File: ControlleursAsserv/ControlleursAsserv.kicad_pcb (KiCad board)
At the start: 4 copper layers, 85 x 56 mm, 100 parts, among them J1 I2C1_5, J10 Codeur, J11 Motor FeedBack, J12 Motor CMD, J13 Codeur, J14 Motor FeedBack, J15 Motor CMD, J16 Codeur, J17 Motor FeedBack, J18 Motor CMD, J2 I2C2_5, J3 CAN1, J4 CAN2, J5 In App Prog, J6 DEBUG, J7 Codeur, J8 Motor CMD, J9 Motor FeedBack, Q1 BSS138, Q10 BSS138, Q11 BSS138, Q12 BSS138, Q13 BSS138, Q14 BSS138, Q2 BSS138, Q3 BSS138, Q4 BSS138, Q5 BSS138, Q6 BSS138, Q7 BSS138, Q8 BSS138, Q9 BSS138, SW1 RESET, SW2 BOOT0, U1 STM32G474RETx, U2 AMS1117-3.3, U3 MCP2558FD-xSN, Y1 16MHz

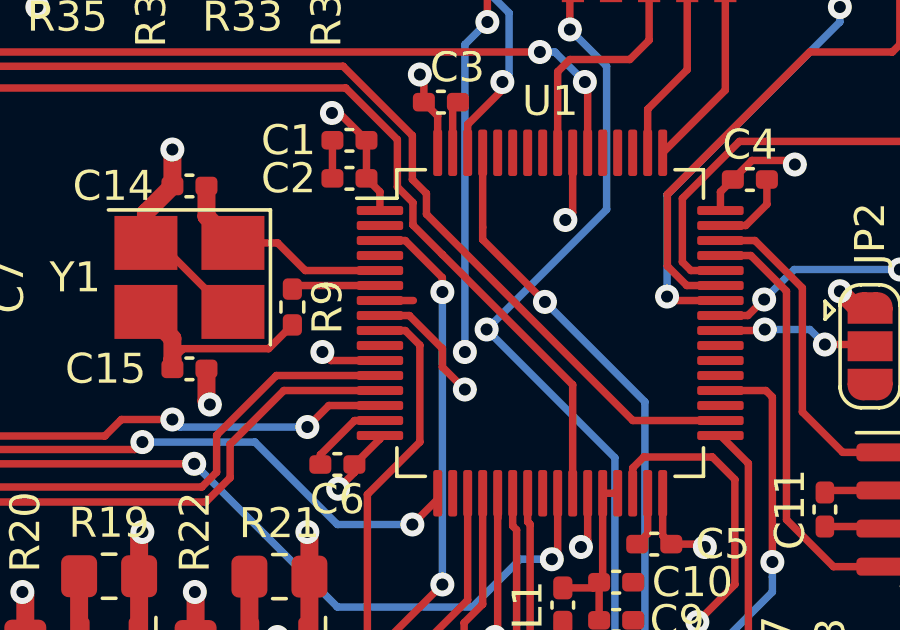
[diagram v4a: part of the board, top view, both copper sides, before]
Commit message: Add size value in layer comments
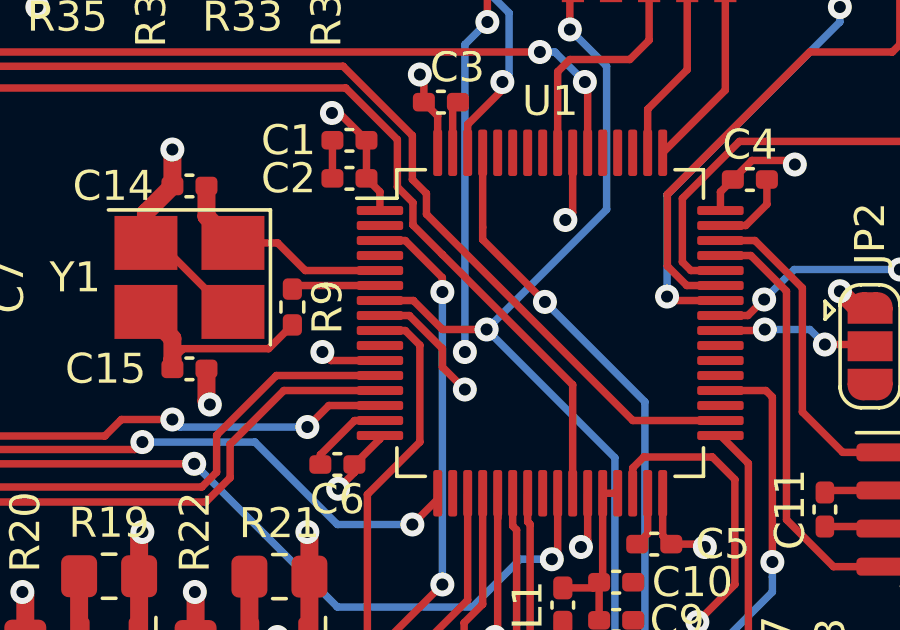
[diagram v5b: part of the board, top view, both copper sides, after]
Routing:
- net RESET: track 53.1 -> 56.0 mm
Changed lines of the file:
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@@
   )
   (dimension (type aligned) (layer "Cmts.User")
-    (pts (xy 145.75 38.75) (xy 145.75 94.75))
-    (height -4.25)
-    (gr_text "56.0000 mm" (at 148.85 66.75 90) (layer "Cmts.User")
+    (pts (xy 64.25 42.25) (xy 64.25 91.25))
+    (height 6.499999)
+    (gr_text "49.0000 mm" (at 56.600001 66.75 90) (layer "Cmts.User")
       (effects (font (size 1 1) (thickness 0.15)))
     )
@@
   )
   (dimension (type aligned) (layer "Cmts.User")
+    (pts (xy 145.75 38.75) (xy 145.75 94.75))
+    (height -11.75)
+    (gr_text "56.0000 mm" (at 156.35 66.75 90) (layer "Cmts.User")
+      (effects (font (size 1 1) (thickness 0.15)))
+    )
+    (format (prefix "") (suffix "") (units 3) (units_format 1) (precision 4))
+    (style (thickness 0.15) (arrow_length 1.27) (text_position_mode 0) (extension_height 0.58642) (extension_offset 0.5) keep_text_aligned)
+  )
+  (dimension (type aligned) (layer "Cmts.User")
+    (pts (xy 64.25 42.25) (xy 122.25 42.25))
+    (height -8)
+    (gr_text "58.0000 mm" (at 93.25 33.1) (layer "Cmts.User")
+      (effects (font (size 1 1) (thickness 0.15)))
+    )
+    (format (prefix "") (suffix "") (units 3) (units_format 1) (precision 4))
+    (style (thickness 0.15) (arrow_length 1.27) (text_position_mode 0) (extension_height 0.58642) (extension_offset 0.5) keep_text_aligned)
+  )
+  (dimension (type aligned) (layer "Cmts.User")
     (pts (xy 60.75 38.75) (xy 145.75 38.75))
-    (height -4.75)
-    (gr_text "85.0000 mm" (at 103.25 32.85) (layer "Cmts.User")
+    (height -10)
+    (gr_text "85.0000 mm" (at 103.25 27.6) (layer "Cmts.User")
       (effects (font (size 1 1) (thickness 0.15)))
     )
@@
   (segment (start 111.169 67.534) (end 112.284 67.534) (width 0.25) (layer "F.Cu") (net 5))
   (segment (start 136.4855 88.42) (end 136.906 88.8405) (width 0.25) (layer "F.Cu") (net 5))
+  (segment (start 113.249019 68.499019) (end 114.725 68.499019) (width 0.25) (layer "F.Cu") (net 5))
   (segment (start 126.0299 86.25) (end 123.75 86.25) (width 0.25) (layer "F.Cu") (net 5))
   (segment (start 117.5 58.5) (end 117.5 56.49) (width 0.25) (layer "F.Cu") (net 5))
+  (segment (start 112.284 67.534) (end 113.249019 68.499019) (width 0.25) (layer "F.Cu") (net 5))
   (segment (start 117.5 56.49) (end 117.602 56.388) (width 0.25) (layer "F.Cu") (net 5))
   (segment (start 128.54 86.25) (end 126.0299 86.25) (width 0.25) (layer "F.Cu") (net 5))

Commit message: Finish Controller Asserv
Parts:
- added C16: 100n, Capacitor_SMD:C_0402_1005Metric_Pad0.74x0.62mm_HandSolder, F.Cu at (131.3, 77.8)
- moved C15 1.32 mm to (103.5, 69.8), turned to 180 degrees
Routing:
- net FAULT_1: track 3.25 -> 60.7 mm, vias 0 -> 3
- net FAULT_2: track 3.25 -> 58.0 mm, vias 0 -> 2
- net SLEEP_3: track 0.00 -> 48.3 mm, vias 0 -> 1
- net PWM_3: track 0.00 -> 39.1 mm, vias 0 -> 1
- net DIR_3: track 0.00 -> 35.8 mm, vias 0 -> 1
- net SLEEP_4: track 0.00 -> 32.8 mm, vias 0 -> 1
- net DIR_1: track 12.5 -> 40.9 mm, vias 0 -> 2
- net CHB_4: track 2.13 -> 28.9 mm, vias 0 -> 2
- net IDX_4: track 2.13 -> 25.5 mm, vias 0 -> 2
- net CHA_4: track 2.13 -> 23.3 mm, vias 0 -> 2
- net GND: track 22.8 -> 42.8 mm, vias 3 -> 8
- net +5V: track 32.9 -> 48.1 mm, vias 13 -> 19
- net PWM_4: track 28.8 -> 25.5 mm, vias 3 -> 1
- net +3.3V: track 120.0 -> 123.3 mm, vias 48 -> 49
- net DIR_4: track 17.0 -> 15.7 mm, vias 2 -> 0
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
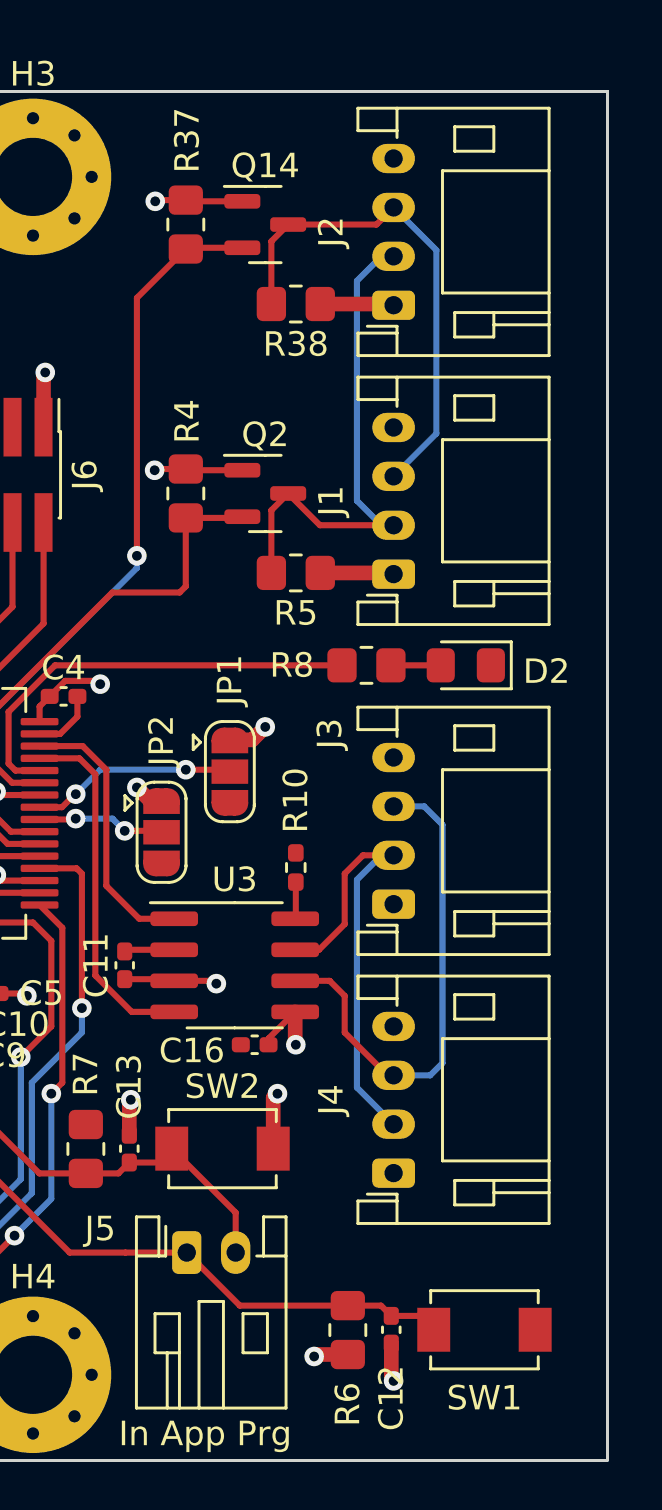
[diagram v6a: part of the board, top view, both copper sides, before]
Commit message: Fix CAN connections to improve routing on ControllerAsserv
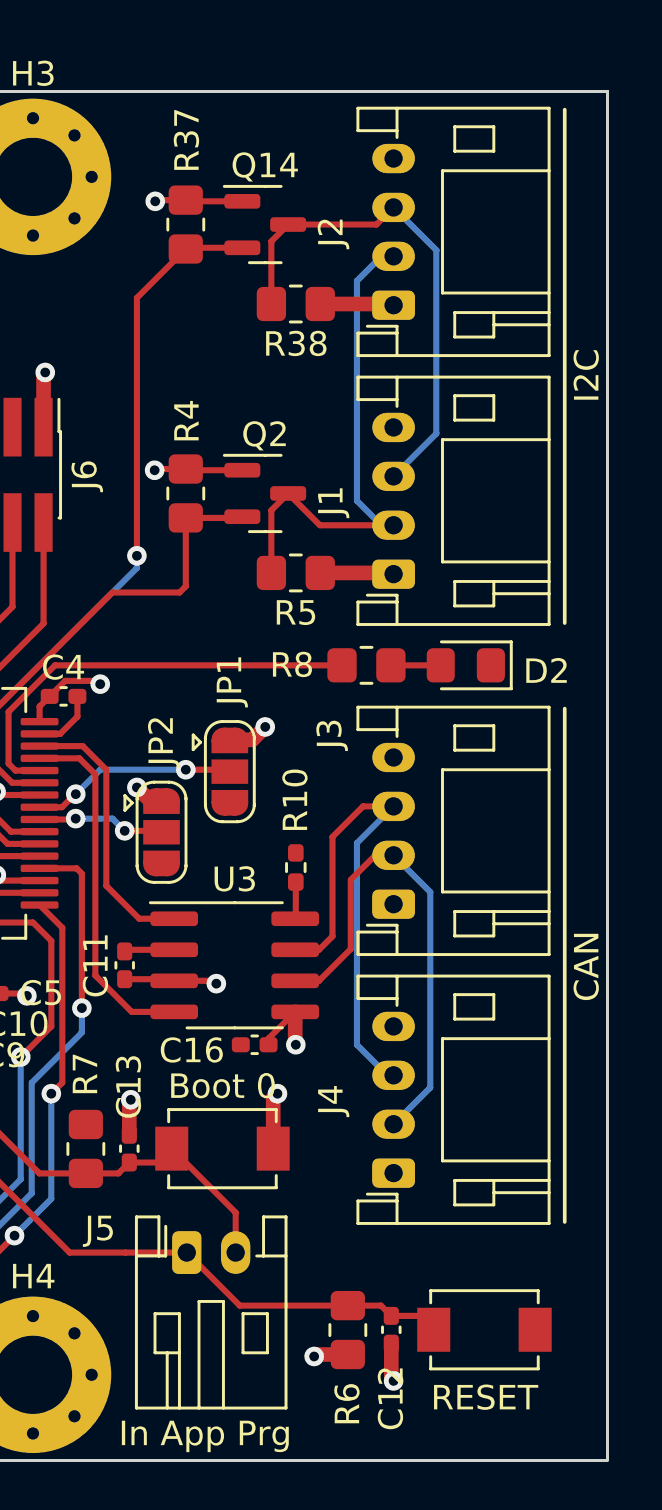
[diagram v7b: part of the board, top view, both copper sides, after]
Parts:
- Boot 0: renamed from SW2
- renumbered SW1 to RESET
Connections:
- U3 pad 6: Net-(J3-Pin_3) -> Net-(J3-Pin_2)
- U3 pad 7: Net-(J3-Pin_2) -> Net-(J3-Pin_3)
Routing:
- net Net-(J3-Pin_2): track 19.4 -> 20.6 mm
- net Net-(J3-Pin_3): track 20.8 -> 21.5 mm
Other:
- board text added: "CAN"
- board text added: "I2C"
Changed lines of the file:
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@@
     (property "ki_keywords" "switch normally-open pushbutton push-button")
     (attr smd)
-    (fp_text reference "SW1" (at 0 -2.794) (layer "F.SilkS")
+    (fp_text reference "RESET" (at 0 -2.794) (layer "F.SilkS")
         (effects (font (size 1 1) (thickness 0.15)))
     )
@@
       (net 1 "+3.3V") (pinfunction "VIO") (pintype "power_in"))
     (pad "6" smd roundrect (at 2.475 0.635) (size 1.95 0.6) (layers "F.Cu" "F.Paste" "F.Mask") (roundrect_rratio 0.25)
-      (net 14 "Net-(J3-Pin_3)") (pinfunction "CANL") (pintype "bidirectional"))
+      (net 13 "Net-(J3-Pin_2)") (pinfunction "CANL") (pintype "bidirectional"))
     (pad "7" smd roundrect (at 2.475 -0.635) (size 1.95 0.6) (layers "F.Cu" "F.Paste" "F.Mask") (roundrect_rratio 0.25)
-      (net 13 "Net-(J3-Pin_2)") (pinfunction "CANH") (pintype "bidirectional"))
+      (net 14 "Net-(J3-Pin_3)") (pinfunction "CANH") (pintype "bidirectional"))
     (pad "8" smd roundrect (at 2.475 -1.905) (size 1.95 0.6) (layers "F.Cu" "F.Paste" "F.Mask") (roundrect_rratio 0.25)
       (net 70 "Net-(U3-S)") (pinfunction "S") (pintype "input"))
@@
     (property "ki_keywords" "switch normally-open pushbutton push-button")
     (attr smd)
-    (fp_text reference "SW2" (at 0 -2.54) (layer "F.SilkS")
+    (fp_text reference "Boot 0" (at 0 -2.54) (layer "F.SilkS")
         (effects (font (size 1 1) (thickness 0.15)))
     )
@@
     )
   )
+  (gr_line (start 144 39.5) (end 144 60.5)
+    (stroke (width 0.15) (type default)) (layer "F.SilkS"))
+  (gr_line (start 144 64) (end 144 85)
+    (stroke (width 0.15) (type default)) (layer "F.SilkS"))
   (gr_rect (start 60.75 38.75) (end 145.75 94.75)
     (stroke (width 0.1) (type default)) (fill none) (layer "Edge.Cuts"))
@@
     (effects (font (size 1 1) (thickness 0.15)) (justify left bottom))
   )
+  (gr_text "CAN" (at 145.5 76 90) (layer "F.SilkS")
+    (effects (font (size 1 1) (thickness 0.15)) (justify left bottom))
+  )
+  (gr_text "I2C" (at 145.5 51.5 90) (layer "F.SilkS")
+    (effects (font (size 1 1) (thickness 0.15)) (justify left bottom))
+  )
   (dimension (type aligned) (layer "Cmts.User")
     (pts (xy 64.25 42.25) (xy 64.25 91.25))
@@
   (segment (start 137 43.5) (end 138.75 45.25) (width 0.25) (layer "B.Cu") (net 12))
   (segment (start 138.75 45.25) (end 138.75 52.75) (width 0.25) (layer "B.Cu") (net 12))
-  (segment (start 135 70.75) (end 135.75 70) (width 0.25) (layer "F.Cu") (net 13))
-  (segment (start 135.75 70) (end 137 70) (width 0.25) (layer "F.Cu") (net 13))
-  (segment (start 135 72.814999) (end 135 70.75) (width 0.25) (layer "F.Cu") (net 13))
-  (segment (start 132.975 73.865) (end 133.949999 73.865) (width 0.25) (layer "F.Cu") (net 13))
-  (segment (start 133.949999 73.865) (end 135 72.814999) (width 0.25) (layer "F.Cu") (net 13))
+  (segment (start 132.975 75.135) (end 133.949999 75.135) (width 0.25) (layer "F.Cu") (net 13))
+  (segment (start 136.25 70) (end 137 70) (width 0.25) (layer "F.Cu") (net 13))
+  (segment (start 135.25 73.834999) (end 135.25 71) (width 0.25) (layer "F.Cu") (net 13))
+  (segment (start 133.949999 75.135) (end 135.25 73.834999) (width 0.25) (layer "F.Cu") (net 13))
+  (segment (start 135.25 71) (end 136.25 70) (width 0.25) (layer "F.Cu") (net 13))
+  (segment (start 138.5 71.5) (end 138.5 79.5) (width 0.25) (layer "B.Cu") (net 13))
   (segment (start 137 70) (end 136.5 70) (width 0.25) (layer "B.Cu") (net 13))
-  (segment (start 135.5 71) (end 135.5 79.5) (width 0.25) (layer "B.Cu") (net 13))
-  (segment (start 136.5 70) (end 135.5 71) (width 0.25) (layer "B.Cu") (net 13))
-  (segment (start 135.5 79.5) (end 137 81) (width 0.25) (layer "B.Cu") (net 13))
-  (segment (start 134.385 75.135) (end 135 75.75) (width 0.25) (layer "F.Cu") (net 14))
-  (segment (start 135 75.75) (end 135 77.25) (width 0.25) (layer "F.Cu") (net 14))
-  (segment (start 135 77.25) (end 136.75 79) (width 0.25) (layer "F.Cu") (net 14))
-  (segment (start 132.975 75.135) (end 134.385 75.135) (width 0.25) (layer "F.Cu") (net 14))
+  (segment (start 137 70) (end 138.5 71.5) (width 0.25) (layer "B.Cu") (net 13))
+  (segment (start 138.5 79.5) (end 137 81) (width 0.25) (layer "B.Cu") (net 13))
+  (segment (start 135.75 68) (end 137 68) (width 0.25) (layer "F.Cu") (net 14))
+  (segment (start 134.5 73.314999) (end 134.5 69.25) (width 0.25) (layer "F.Cu") (net 14))
+  (segment (start 133.949999 73.865) (end 134.5 73.314999) (width 0.25) (layer "F.Cu") (net 14))
+  (segment (start 132.975 73.865) (end 133.949999 73.865) (width 0.25) (layer "F.Cu") (net 14))
+  (segment (start 134.5 69.25) (end 135.75 68) (width 0.25) (layer "F.Cu") (net 14))
   (segment (start 136.75 79) (end 137 79) (width 0.25) (layer "F.Cu") (net 14))
-  (segment (start 139 68.75) (end 139 78.5) (width 0.25) (layer "B.Cu") (net 14))
-  (segment (start 139 78.5) (end 138.5 79) (width 0.25) (layer "B.Cu") (net 14))
-  (segment (start 137 68) (end 138.25 68) (width 0.25) (layer "B.Cu") (net 14))
-  (segment (start 138.25 68) (end 139 68.75) (width 0.25) (layer "B.Cu") (net 14))
-  (segment (start 138.5 79) (end 137 79) (width 0.25) (layer "B.Cu") (net 14))
+  (segment (start 137 68) (end 135.5 69.5) (width 0.25) (layer "B.Cu") (net 14))
+  (segment (start 135.5 69.5) (end 135.5 77.75) (width 0.25) (layer "B.Cu") (net 14))
+  (segment (start 135.5 77.75) (end 136.75 79) (width 0.25) (layer "B.Cu") (net 14))
+  (segment (start 136.75 79) (end 137 79) (width 0.25) (layer "B.Cu") (net 14))
   (segment (start 122.682 56.388) (end 122.682 60.521) (width 0.25) (layer "F.Cu") (net 15))
   (segment (start 122.682 60.521) (end 120.594 62.609) (width 0.25) (layer "F.Cu") (net 15))

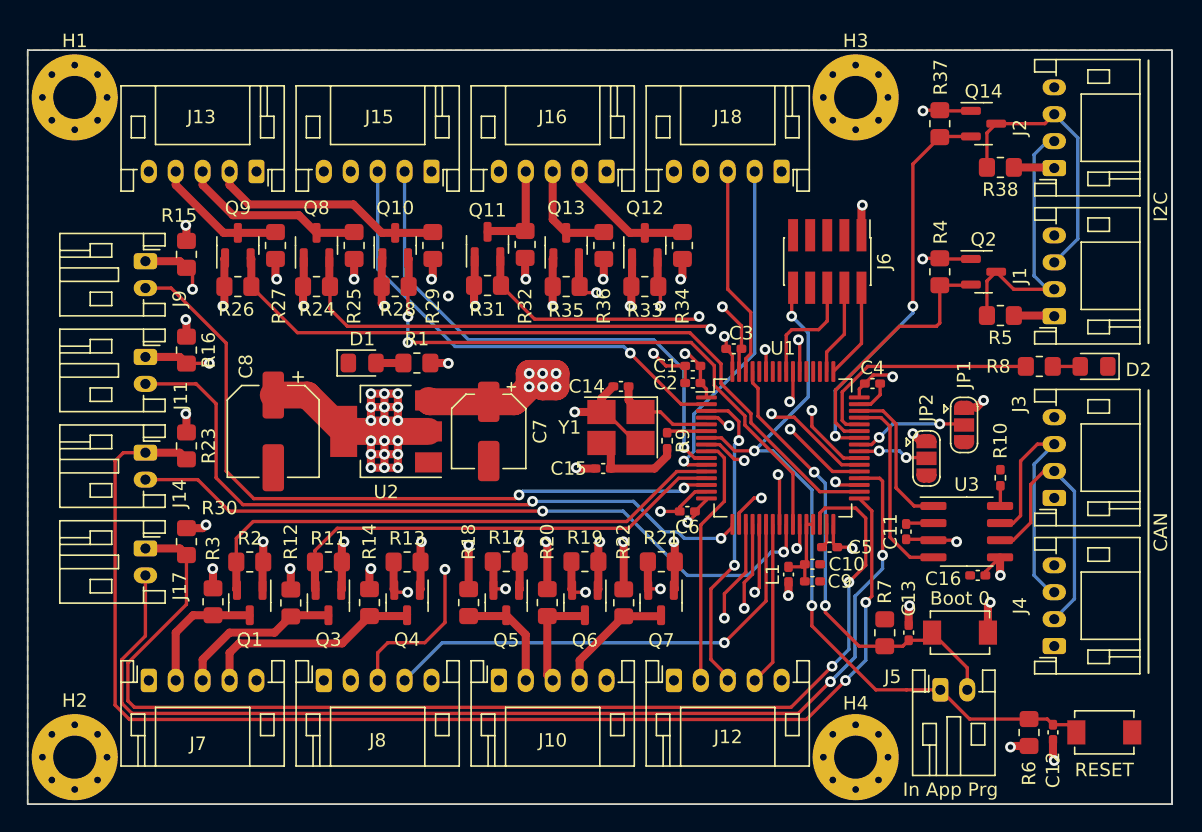
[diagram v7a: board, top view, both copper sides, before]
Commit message: Upgrade to KicCad 8
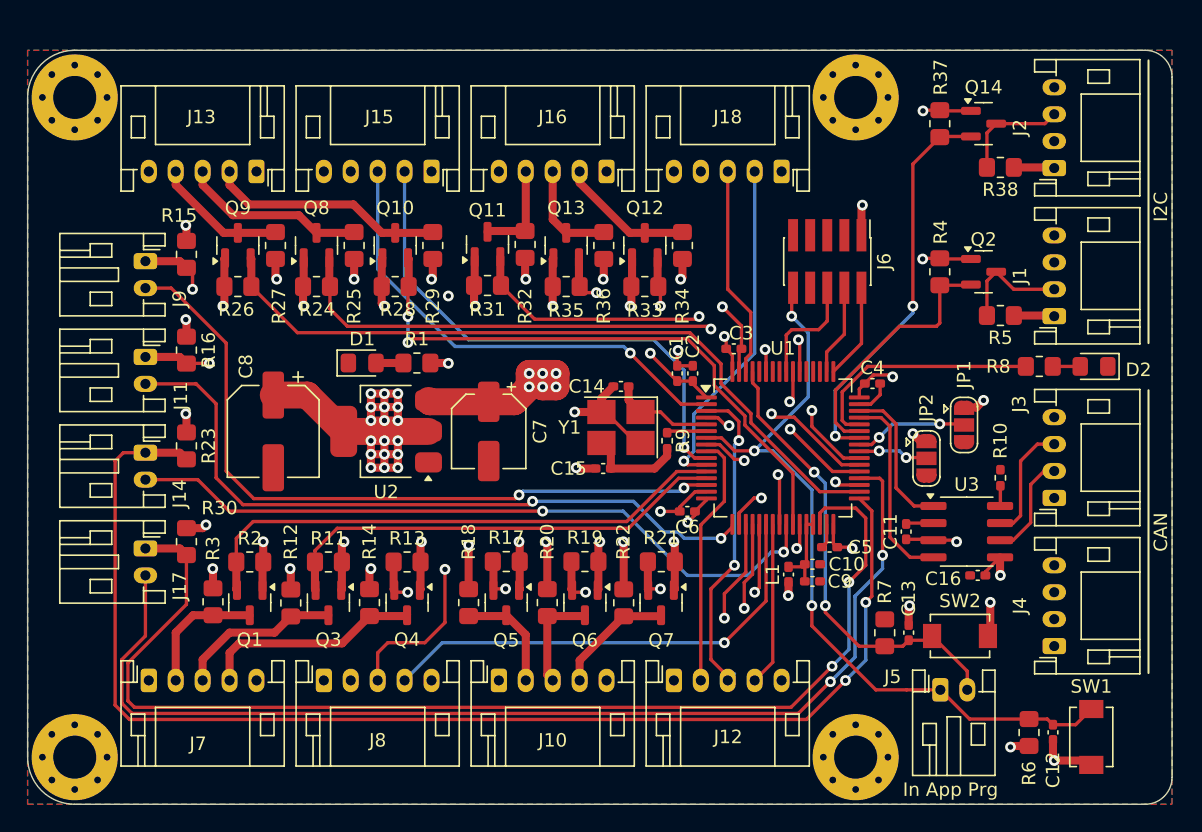
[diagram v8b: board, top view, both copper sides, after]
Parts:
- removed Boot 0: BOOT0, ARIG:SW_TS_1088_AR_3x4x2
- removed RESET: RESET, ARIG:SW_TS_1088_AR_3x4x2
- added SW1: RESET, ARIG:SW_TS_1088_AR_3x4x2, F.Cu at (139.8, 89.8)
- added SW2: BOOT0, ARIG:SW_TS_1088_AR_3x4x2, F.Cu at (130.0, 82.2)
- moved C1 1.28 mm to (109.0, 62.8), turned to 90 degrees
- moved C2 0.71 mm to (110.2, 62.8), turned to 90 degrees
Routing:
- net +3.3V: track 123.3 -> 125.2 mm
- net RESET: track 56.8 -> 58.1 mm
- net GND: track 42.8 -> 44.0 mm
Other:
- outline, holes or cut-outs redrawn
